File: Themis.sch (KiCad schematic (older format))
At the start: 47 parts, among them J1 SMA, J10 Conn_01x01, J11 Conn_01x01, J12 Conn_01x01, J13 Conn_01x01, J14 SMA, J15 SMA, J16 SMA, J17 SMA, J18 Conn_01x01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

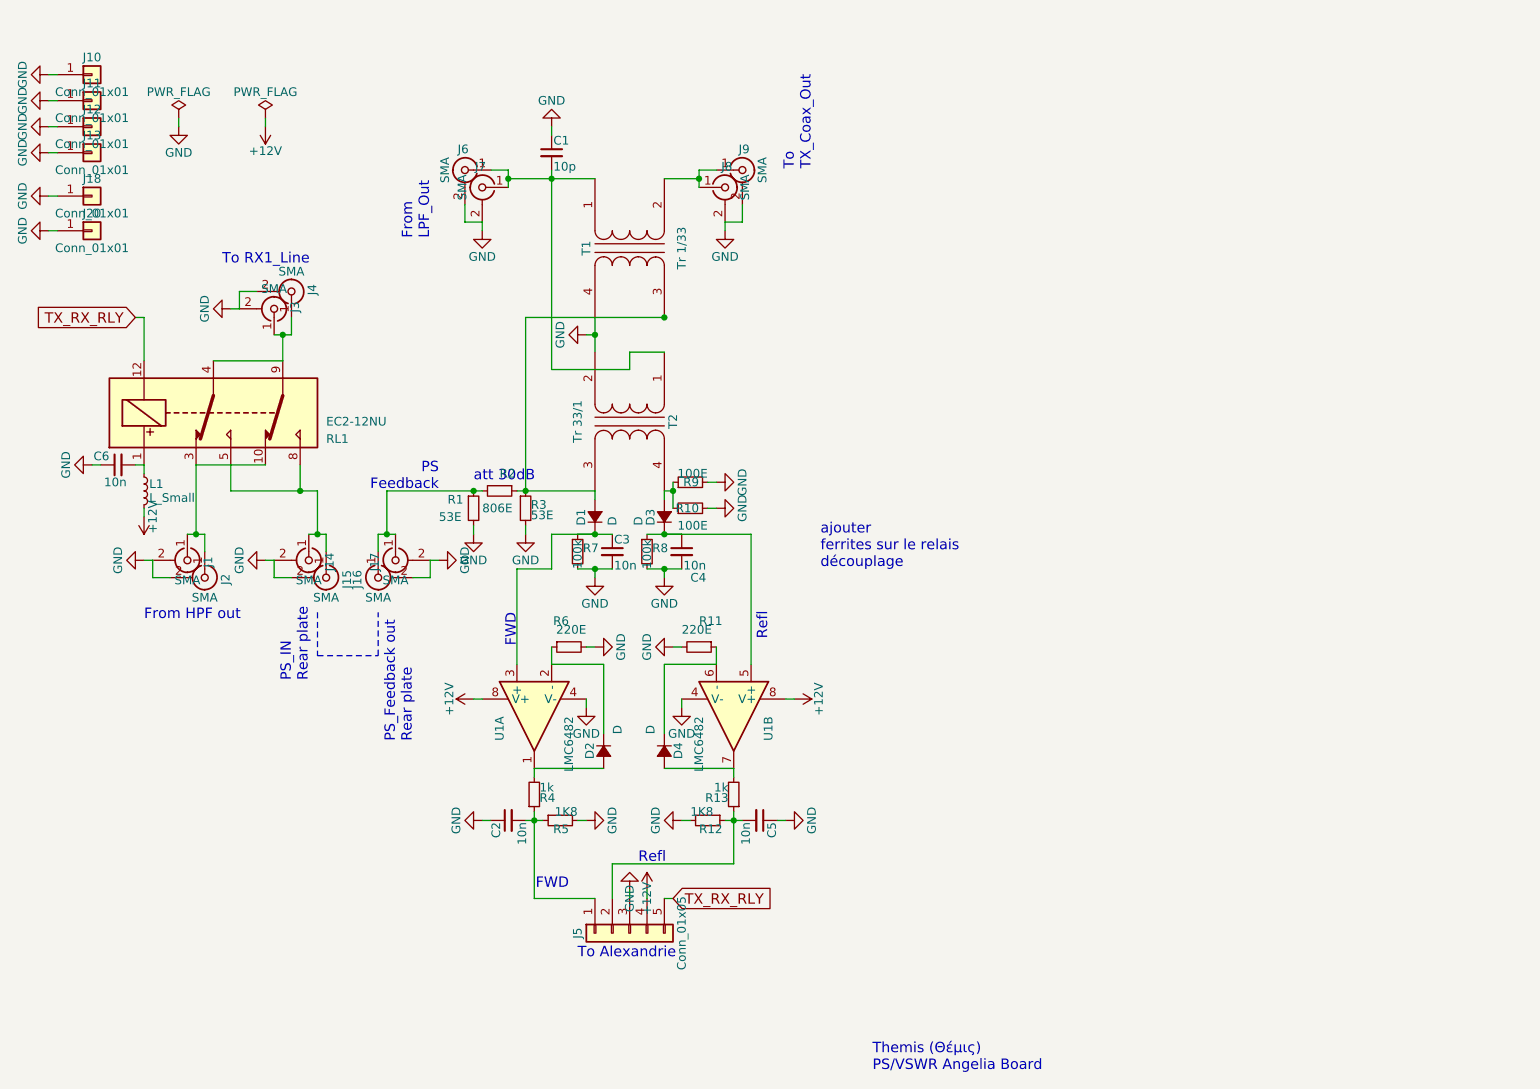
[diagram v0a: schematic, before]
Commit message: BAT54 and transformer shielding added
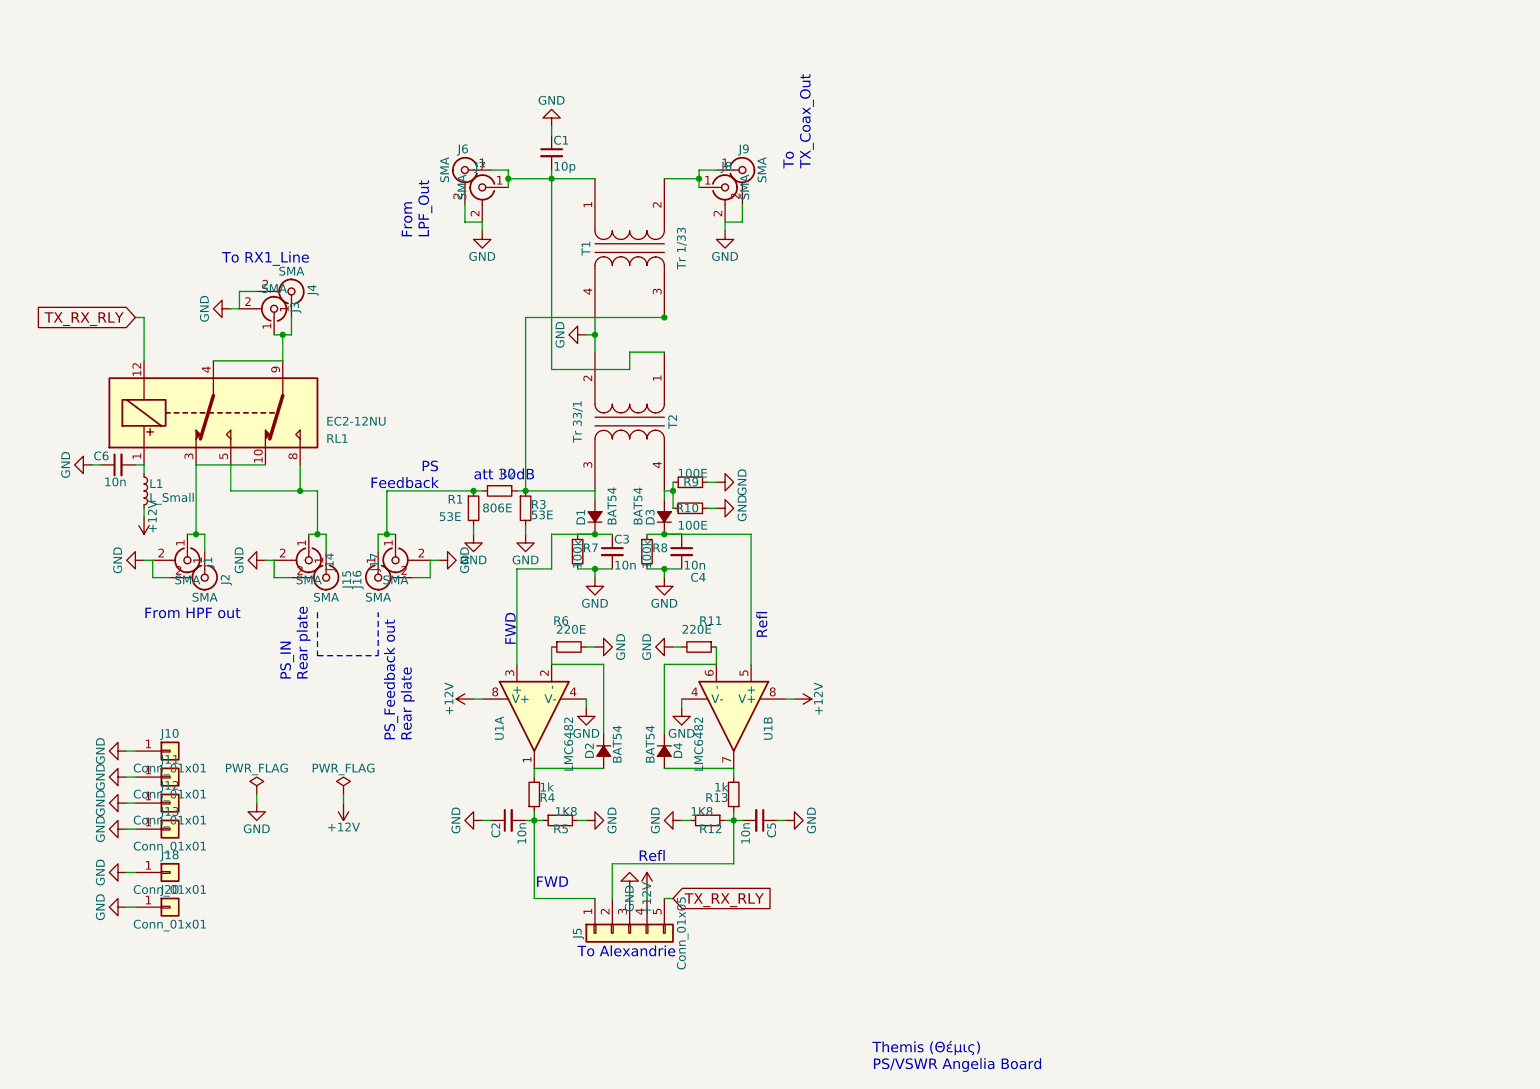
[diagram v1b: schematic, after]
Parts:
- D1, D2, D3, D4: value D -> BAT54; footprint Diodes_SMD:D_1206 -> Diodes_SMD:D_SOT-23_ANK
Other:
- note removed: "ajouter \nferrites sur le relais\ndécouplage \n"
- moved on the sheet: J10, J11, J12, J13, J18, J20
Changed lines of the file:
@@
 L GND #PWR02
 U 1 1 5A4CED7A
-P 3300 1350
-F 0 "#PWR02" H 3300 1100 50  0001 C CNN
-F 1 "GND" H 3300 1200 50  0000 C CNN
-F 2 "" H 3300 1350 50  0001 C CNN
-F 3 "" H 3300 1350 50  0001 C CNN
-	1    3300 1350
+P 3750 5250
+F 0 "#PWR02" H 3750 5000 50  0001 C CNN
+F 1 "GND" H 3750 5100 50  0000 C CNN
+F 2 "" H 3750 5250 50  0001 C CNN
+F 3 "" H 3750 5250 50  0001 C CNN
+	1    3750 5250
 	1    0    0    -1
 $EndComp
@@
 L PWR_FLAG #FLG03
 U 1 1 5A4CED92
-P 3800 1300
-F 0 "#FLG03" H 3800 1375 50  0001 C CNN
-F 1 "PWR_FLAG" H 3800 1450 50  0000 C CNN
-F 2 "" H 3800 1300 50  0001 C CNN
-F 3 "" H 3800 1300 50  0001 C CNN
-	1    3800 1300
+P 4250 5200
+F 0 "#FLG03" H 4250 5275 50  0001 C CNN
+F 1 "PWR_FLAG" H 4250 5350 50  0000 C CNN
+F 2 "" H 4250 5200 50  0001 C CNN
+F 3 "" H 4250 5200 50  0001 C CNN
+	1    4250 5200
 	1    0    0    -1
 $EndComp
@@
 L +12V #PWR04
 U 1 1 5A4CEDCA
-P 3800 1350
-F 0 "#PWR04" H 3800 1200 50  0001 C CNN
-F 1 "+12V" H 3800 1490 50  0000 C CNN
-F 2 "" H 3800 1350 50  0001 C CNN
-F 3 "" H 3800 1350 50  0001 C CNN
-	1    3800 1350
+P 4250 5250
+F 0 "#PWR04" H 4250 5100 50  0001 C CNN
+F 1 "+12V" H 4250 5390 50  0000 C CNN
+F 2 "" H 4250 5250 50  0001 C CNN
+F 3 "" H 4250 5250 50  0001 C CNN
+	1    4250 5250
 	-1   0    0    1
 $EndComp
@@
 P 5700 3600
 F 0 "D1" H 5650 3680 50  0000 L CNN
-F 1 "D" H 5650 3500 50  0000 L CNN
-F 2 "Diodes_SMD:D_1206" V 5700 3600 50  0001 C CNN
+F 1 "BAT54" H 5650 3500 50  0000 L CNN
+F 2 "Diodes_SMD:D_SOT-23_ANK" V 5700 3600 50  0001 C CNN
 F 3 "" V 5700 3600 50  0001 C CNN
 	1    5700 3600
@@
 P 6100 3600
 F 0 "D3" H 6050 3680 50  0000 L CNN
-F 1 "D" H 6050 3750 50  0000 L CNN
-F 2 "Diodes_SMD:D_1206" V 6100 3600 50  0001 C CNN
+F 1 "BAT54" H 6050 3750 50  0000 L CNN
+F 2 "Diodes_SMD:D_SOT-23_ANK" V 6100 3600 50  0001 C CNN
 F 3 "" V 6100 3600 50  0001 C CNN
 	1    6100 3600
@@
 P 6100 4950
 F 0 "D4" H 6050 5030 50  0000 L CNN
-F 1 "D" H 5950 4870 50  0000 L CNN
-F 2 "Diodes_SMD:D_1206" V 6100 4950 50  0001 C CNN
+F 1 "BAT54" H 5950 4870 50  0000 L CNN
+F 2 "Diodes_SMD:D_SOT-23_ANK" V 6100 4950 50  0001 C CNN
 F 3 "" V 6100 4950 50  0001 C CNN
 	1    6100 4950
@@
 P 5750 4950
 F 0 "D2" H 5700 5030 50  0000 L CNN
-F 1 "D" H 5600 4870 50  0000 L CNN
-F 2 "Diodes_SMD:D_1206" V 5750 4950 50  0001 C CNN
+F 1 "BAT54" H 5600 4870 50  0000 L CNN
+F 2 "Diodes_SMD:D_SOT-23_ANK" V 5750 4950 50  0001 C CNN
 F 3 "" V 5750 4950 50  0001 C CNN
 	1    5750 4950
@@
 L PWR_FLAG #FLG026
 U 1 1 5A4D8E5C
-P 3300 1300
-F 0 "#FLG026" H 3300 1375 50  0001 C CNN
-F 1 "PWR_FLAG" H 3300 1450 50  0000 C CNN
-F 2 "" H 3300 1300 50  0001 C CNN
-F 3 "" H 3300 1300 50  0001 C CNN
-	1    3300 1300
-	1    0    0    -1
-$EndComp
-Wire Wire Line
-	3300 1300 3300 1350
-Wire Wire Line
-	3800 1300 3800 1350
+P 3750 5200
+F 0 "#FLG026" H 3750 5275 50  0001 C CNN
+F 1 "PWR_FLAG" H 3750 5350 50  0000 C CNN
+F 2 "" H 3750 5200 50  0001 C CNN
+F 3 "" H 3750 5200 50  0001 C CNN
+	1    3750 5200
+	1    0    0    -1
+$EndComp
+Wire Wire Line
+	3750 5200 3750 5250
+Wire Wire Line
+	4250 5200 4250 5250
 $Comp
 L Conn_Coaxial J8
@@
 L Conn_01x01 J13
 U 1 1 5A4DCC25
-P 2800 1500
-F 0 "J13" H 2800 1600 50  0000 C CNN
-F 1 "Conn_01x01" H 2800 1400 50  0000 C CNN
-F 2 "MountingHole:MountingHole_3.2mm_M3_DIN965_Pad" H 2800 1500 50  0001 C CNN
-F 3 "" H 2800 1500 50  0001 C CNN
-	1    2800 1500
+P 3250 5400
+F 0 "J13" H 3250 5500 50  0000 C CNN
+F 1 "Conn_01x01" H 3250 5300 50  0000 C CNN
+F 2 "MountingHole:MountingHole_3.2mm_M3_DIN965_Pad" H 3250 5400 50  0001 C CNN
+F 3 "" H 3250 5400 50  0001 C CNN
+	1    3250 5400
 	1    0    0    -1
 $EndComp
@@
 L GND #PWR030
 U 1 1 5A4DCFB7
-P 2550 1500
-F 0 "#PWR030" H 2550 1250 50  0001 C CNN
-F 1 "GND" H 2550 1350 50  0000 C CNN
-F 2 "" H 2550 1500 50  0001 C CNN
-F 3 "" H 2550 1500 50  0001 C CNN
-	1    2550 1500
+P 3000 5400
+F 0 "#PWR030" H 3000 5150 50  0001 C CNN
+F 1 "GND" H 3000 5250 50  0000 C CNN
+F 2 "" H 3000 5400 50  0001 C CNN
+F 3 "" H 3000 5400 50  0001 C CNN
+	1    3000 5400
 	0    1    -1   0
 $EndComp
 Wire Wire Line
-	2600 1500 2550 1500
+	3050 5400 3000 5400
 $Comp
 L Conn_01x01 J12
 U 1 1 5A4DD05C
-P 2800 1350
-F 0 "J12" H 2800 1450 50  0000 C CNN
-F 1 "Conn_01x01" H 2800 1250 50  0000 C CNN
-F 2 "MountingHole:MountingHole_3.2mm_M3_DIN965_Pad" H 2800 1350 50  0001 C CNN
-F 3 "" H 2800 1350 50  0001 C CNN
-	1    2800 1350
+P 3250 5250
+F 0 "J12" H 3250 5350 50  0000 C CNN
+F 1 "Conn_01x01" H 3250 5150 50  0000 C CNN
+F 2 "MountingHole:MountingHole_3.2mm_M3_DIN965_Pad" H 3250 5250 50  0001 C CNN
+F 3 "" H 3250 5250 50  0001 C CNN
+	1    3250 5250
 	1    0    0    -1
 $EndComp
@@
 L GND #PWR031
 U 1 1 5A4DD062
-P 2550 1350
-F 0 "#PWR031" H 2550 1100 50  0001 C CNN
-F 1 "GND" H 2550 1200 50  0000 C CNN
-F 2 "" H 2550 1350 50  0001 C CNN
-F 3 "" H 2550 1350 50  0001 C CNN
-	1    2550 1350
+P 3000 5250
+F 0 "#PWR031" H 3000 5000 50  0001 C CNN
+F 1 "GND" H 3000 5100 50  0000 C CNN
+F 2 "" H 3000 5250 50  0001 C CNN
+F 3 "" H 3000 5250 50  0001 C CNN
+	1    3000 5250
 	0    1    -1   0
 $EndComp
 Wire Wire Line
-	2600 1350 2550 1350
+	3050 5250 3000 5250
 $Comp
 L Conn_01x01 J11
 U 1 1 5A4DD0B3
-P 2800 1200
-F 0 "J11" H 2800 1300 50  0000 C CNN
-F 1 "Conn_01x01" H 2800 1100 50  0000 C CNN
-F 2 "MountingHole:MountingHole_3.2mm_M3_DIN965_Pad" H 2800 1200 50  0001 C CNN
-F 3 "" H 2800 1200 50  0001 C CNN
-	1    2800 1200
+P 3250 5100
+F 0 "J11" H 3250 5200 50  0000 C CNN
+F 1 "Conn_01x01" H 3250 5000 50  0000 C CNN
+F 2 "MountingHole:MountingHole_3.2mm_M3_DIN965_Pad" H 3250 5100 50  0001 C CNN
+F 3 "" H 3250 5100 50  0001 C CNN
+	1    3250 5100
 	1    0    0    -1
 $EndComp
@@
 L GND #PWR032
 U 1 1 5A4DD0B9
-P 2550 1200
-F 0 "#PWR032" H 2550 950 50  0001 C CNN
-F 1 "GND" H 2550 1050 50  0000 C CNN
-F 2 "" H 2550 1200 50  0001 C CNN
-F 3 "" H 2550 1200 50  0001 C CNN
-	1    2550 1200
+P 3000 5100
+F 0 "#PWR032" H 3000 4850 50  0001 C CNN
+F 1 "GND" H 3000 4950 50  0000 C CNN
+F 2 "" H 3000 5100 50  0001 C CNN
+F 3 "" H 3000 5100 50  0001 C CNN
+	1    3000 5100
 	0    1    -1   0
 $EndComp
 Wire Wire Line
-	2600 1200 2550 1200
+	3050 5100 3000 5100
 $Comp
 L Conn_01x01 J10
 U 1 1 5A4DD0C0
-P 2800 1050
-F 0 "J10" H 2800 1150 50  0000 C CNN
-F 1 "Conn_01x01" H 2800 950 50  0000 C CNN
-F 2 "MountingHole:MountingHole_3.2mm_M3_DIN965_Pad" H 2800 1050 50  0001 C CNN
-F 3 "" H 2800 1050 50  0001 C CNN
-	1    2800 1050
+P 3250 4950
+F 0 "J10" H 3250 5050 50  0000 C CNN
+F 1 "Conn_01x01" H 3250 4850 50  0000 C CNN
+F 2 "MountingHole:MountingHole_3.2mm_M3_DIN965_Pad" H 3250 4950 50  0001 C CNN
+F 3 "" H 3250 4950 50  0001 C CNN
+	1    3250 4950
 	1    0    0    -1
 $EndComp
@@
 L GND #PWR033
 U 1 1 5A4DD0C6
-P 2550 1050
-F 0 "#PWR033" H 2550 800 50  0001 C CNN
-F 1 "GND" H 2550 900 50  0000 C CNN
-F 2 "" H 2550 1050 50  0001 C CNN
-F 3 "" H 2550 1050 50  0001 C CNN
-	1    2550 1050
+P 3000 4950
+F 0 "#PWR033" H 3000 4700 50  0001 C CNN
+F 1 "GND" H 3000 4800 50  0000 C CNN
+F 2 "" H 3000 4950 50  0001 C CNN
+F 3 "" H 3000 4950 50  0001 C CNN
+	1    3000 4950
 	0    1    -1   0
 $EndComp
 Wire Wire Line
-	2600 1050 2550 1050
+	3050 4950 3000 4950
 $Comp
 L GND #PWR034
@@
 Text Notes 5550 5750 2    60   ~ 0
 FWD\n
-Text Notes 7000 3900 0    60   ~ 0
-ajouter \nferrites sur le relais\ndécouplage \n
 $Comp
 L C_Small C6
@@
 L Conn_01x01 J20
 U 1 1 5A4E5EFB
-P 2800 1950
-F 0 "J20" H 2800 2050 50  0000 C CNN
-F 1 "Conn_01x01" H 2800 1850 50  0000 C CNN
-F 2 "MountingHole:MountingHole_3.2mm_M3_DIN965_Pad" H 2800 1950 50  0001 C CNN
-F 3 "" H 2800 1950 50  0001 C CNN
-	1    2800 1950
+P 3250 5850
+F 0 "J20" H 3250 5950 50  0000 C CNN
+F 1 "Conn_01x01" H 3250 5750 50  0000 C CNN
+F 2 "MountingHole:MountingHole_3.2mm_M3_DIN965_Pad" H 3250 5850 50  0001 C CNN
+F 3 "" H 3250 5850 50  0001 C CNN
+	1    3250 5850
 	1    0    0    -1
 $EndComp
@@
 L GND #PWR037
 U 1 1 5A4E5F01
-P 2550 1950
-F 0 "#PWR037" H 2550 1700 50  0001 C CNN
-F 1 "GND" H 2550 1800 50  0000 C CNN
-F 2 "" H 2550 1950 50  0001 C CNN
-F 3 "" H 2550 1950 50  0001 C CNN
-	1    2550 1950
+P 3000 5850
+F 0 "#PWR037" H 3000 5600 50  0001 C CNN
+F 1 "GND" H 3000 5700 50  0000 C CNN
+F 2 "" H 3000 5850 50  0001 C CNN
+F 3 "" H 3000 5850 50  0001 C CNN
+	1    3000 5850
 	0    1    -1   0
 $EndComp
 Wire Wire Line
-	2600 1950 2550 1950
+	3050 5850 3000 5850
 $Comp
 L Conn_01x01 J18
 U 1 1 5A4E5F15
-P 2800 1750
-F 0 "J18" H 2800 1850 50  0000 C CNN
-F 1 "Conn_01x01" H 2800 1650 50  0000 C CNN
-F 2 "MountingHole:MountingHole_3.2mm_M3_DIN965_Pad" H 2800 1750 50  0001 C CNN
-F 3 "" H 2800 1750 50  0001 C CNN
-	1    2800 1750
+P 3250 5650
+F 0 "J18" H 3250 5750 50  0000 C CNN
+F 1 "Conn_01x01" H 3250 5550 50  0000 C CNN
+F 2 "MountingHole:MountingHole_3.2mm_M3_DIN965_Pad" H 3250 5650 50  0001 C CNN
+F 3 "" H 3250 5650 50  0001 C CNN
+	1    3250 5650
 	1    0    0    -1
 $EndComp
@@
 L GND #PWR038
 U 1 1 5A4E5F1B
-P 2550 1750
-F 0 "#PWR038" H 2550 1500 50  0001 C CNN
-F 1 "GND" H 2550 1600 50  0000 C CNN
-F 2 "" H 2550 1750 50  0001 C CNN
-F 3 "" H 2550 1750 50  0001 C CNN
-	1    2550 1750
+P 3000 5650
+F 0 "#PWR038" H 3000 5400 50  0001 C CNN
+F 1 "GND" H 3000 5500 50  0000 C CNN
+F 2 "" H 3000 5650 50  0001 C CNN
+F 3 "" H 3000 5650 50  0001 C CNN
+	1    3000 5650
 	0    1    -1   0
 $EndComp
 Wire Wire Line
-	2600 1750 2550 1750
+	3050 5650 3000 5650
 $EndSCHEMATC

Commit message: ajout ss rep
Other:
- note added: "from HPF out"
- note removed: "From HPF out"
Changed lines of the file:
@@
 	6450 1900 6450 1950
 Text Notes 3100 4200 0    60   ~ 0
-From HPF out
+from  HPF out
 Text Notes 3550 2150 0    60   ~ 0
 To RX1_Line
@@
 Wire Wire Line
 	3050 5650 3000 5650
+Text Notes 3950 3650 2    60   ~ 0
+PS\nFeedback\n
 $EndSCHEMATC

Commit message: temporary update
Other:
- note added: "28B0562-100\nlaird"
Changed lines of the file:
@@
 EESchema Schematic File Version 2
+LIBS:ee2-5nu
+LIBS:Amplifier_Operational
+LIBS:Connector_Generic
+LIBS:Device
 LIBS:power
-LIBS:device
-LIBS:relays
-LIBS:conn
-LIBS:linear
-LIBS:ee2-5nu
+LIBS:Regulator_Linear
 LIBS:Themis-cache
 EELAYER 25 0
@@
 Text Notes 3950 3650 2    60   ~ 0
 PS\nFeedback\n
+Text Notes 8100 1550 0    60   ~ 0
+28B0562-100\nlaird
 $EndSCHEMATC

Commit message: en route pour la version 2.0
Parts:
- removed C6: 10n, Capacitors_SMD:C_0805_HandSoldering, symbol C_Small
- removed J1, J14, J3, J6: SMA, SMA_PINS:SMA_EDGE_NRW, symbol Conn_Coaxial
- removed J15, J16, J2, J4, J9: SMA, SMA_PINS:SMA_PINS, symbol Conn_Coaxial
- removed L1: L_Small, Inductors_SMD:L_0805_HandSoldering, symbol L_Small
- removed RL1: EC2-12NU, 2_Form_C_Relay:Relay_DPDT_NEC_EC2, symbol EC2-12NU
- added D? (x2): BZX84C3V3LT116, symbol D_Zener
- R11, R6: value 220E -> 220k
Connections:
- net GND: now also D?.2 (A), D?.2 (A)
- net at C5.2, J5.2 (Pin_2), R12.1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: now also D?.1 (K)
- net at C2.2, J5.1 (Pin_1), R4.1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: now also D?.1 (K)
- net TX_RX_RLY: no longer names the net of J5.5 (Pin_5)
- no-connect marks 0 -> 1
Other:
- note removed: "PS\nFeedback\n"
- note removed: "PS_IN\nRear plate"
- note removed: "To RX1_Line"
- note removed: "from HPF out"
- moved on the sheet: C2, C3, C4, C5, D1, D2, D3, D4, J10, J11, J12, J13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
